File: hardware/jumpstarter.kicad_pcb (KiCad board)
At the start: 4 copper layers, 170 x 170 mm, 148 parts, among them J1 USB_C_Receptacle_PowerOnly_6P, J10 Conn_01x02_Pin, J11 Conn_01x02_Pin, J12 Conn_01x02_Pin, J13 Conn_01x02_Pin, J14 Conn_01x02_Pin, J15 Conn_01x02_Pin, J16 Conn_01x02_Pin, J2 Barrel_Jack_MountingPin, J3 Barrel_Jack_MountingPin, J4 Conn_01x09_Pin, J5 USB_C_Receptacle_PowerOnly_6P, J6 Conn_01x05_Pin, J7 USB3_B, J8 USB3_B_Micro, J9 USB3_A, P1 USB_C_Plug_USB2.0, Q1 FDC6330L, Q2 FDC6330L, Q3 FDC6330L, Q4 FDC6330L, SW1 SW_Push, SW2 SW_Push, SW3 SW_Push, U1 STM32F411CEUx, U2 AP2127N-3.3, U3 AP2127N-3.3, U4 ACS725LLCTR-05AB-T, U6 TMUXHS4212, Y2 25 Mhz Crystal

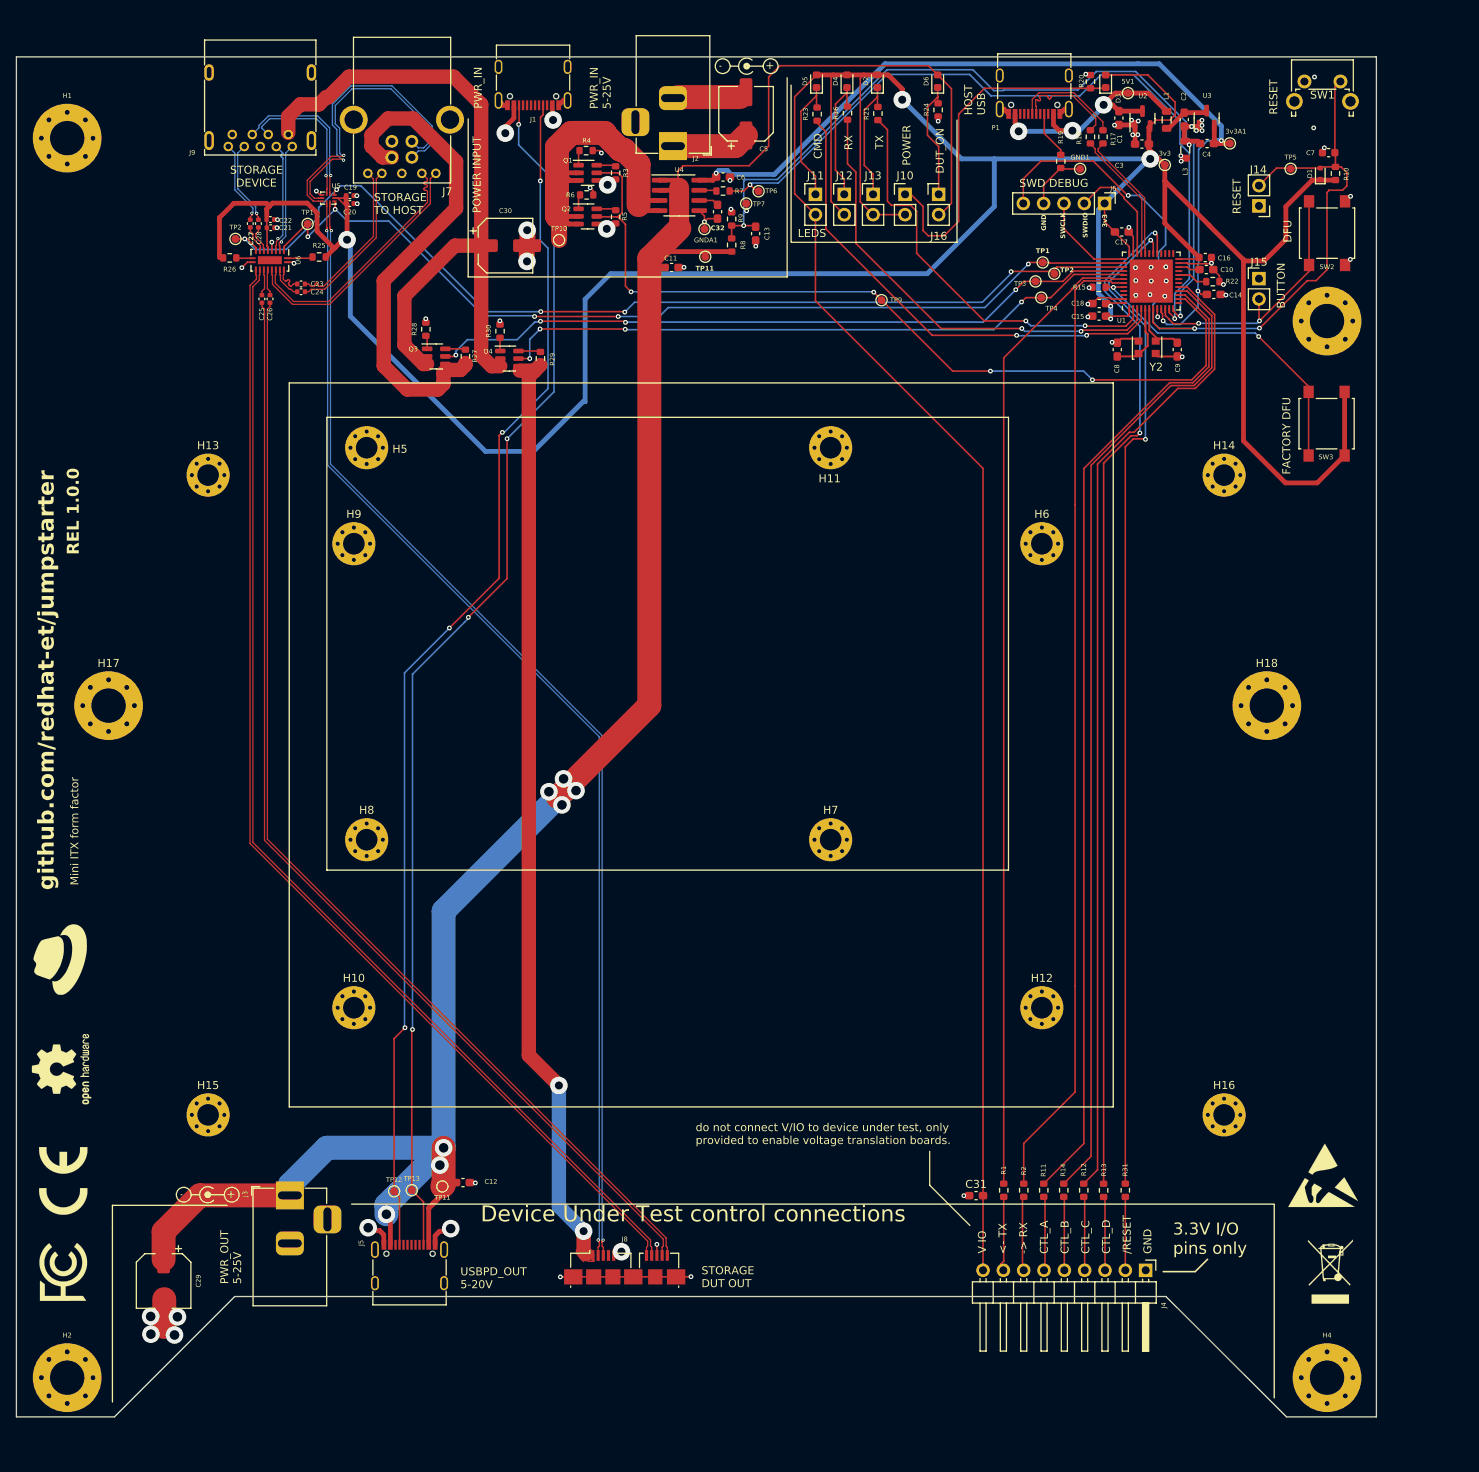
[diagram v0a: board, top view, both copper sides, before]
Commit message: Started routing USB3 diff pairs
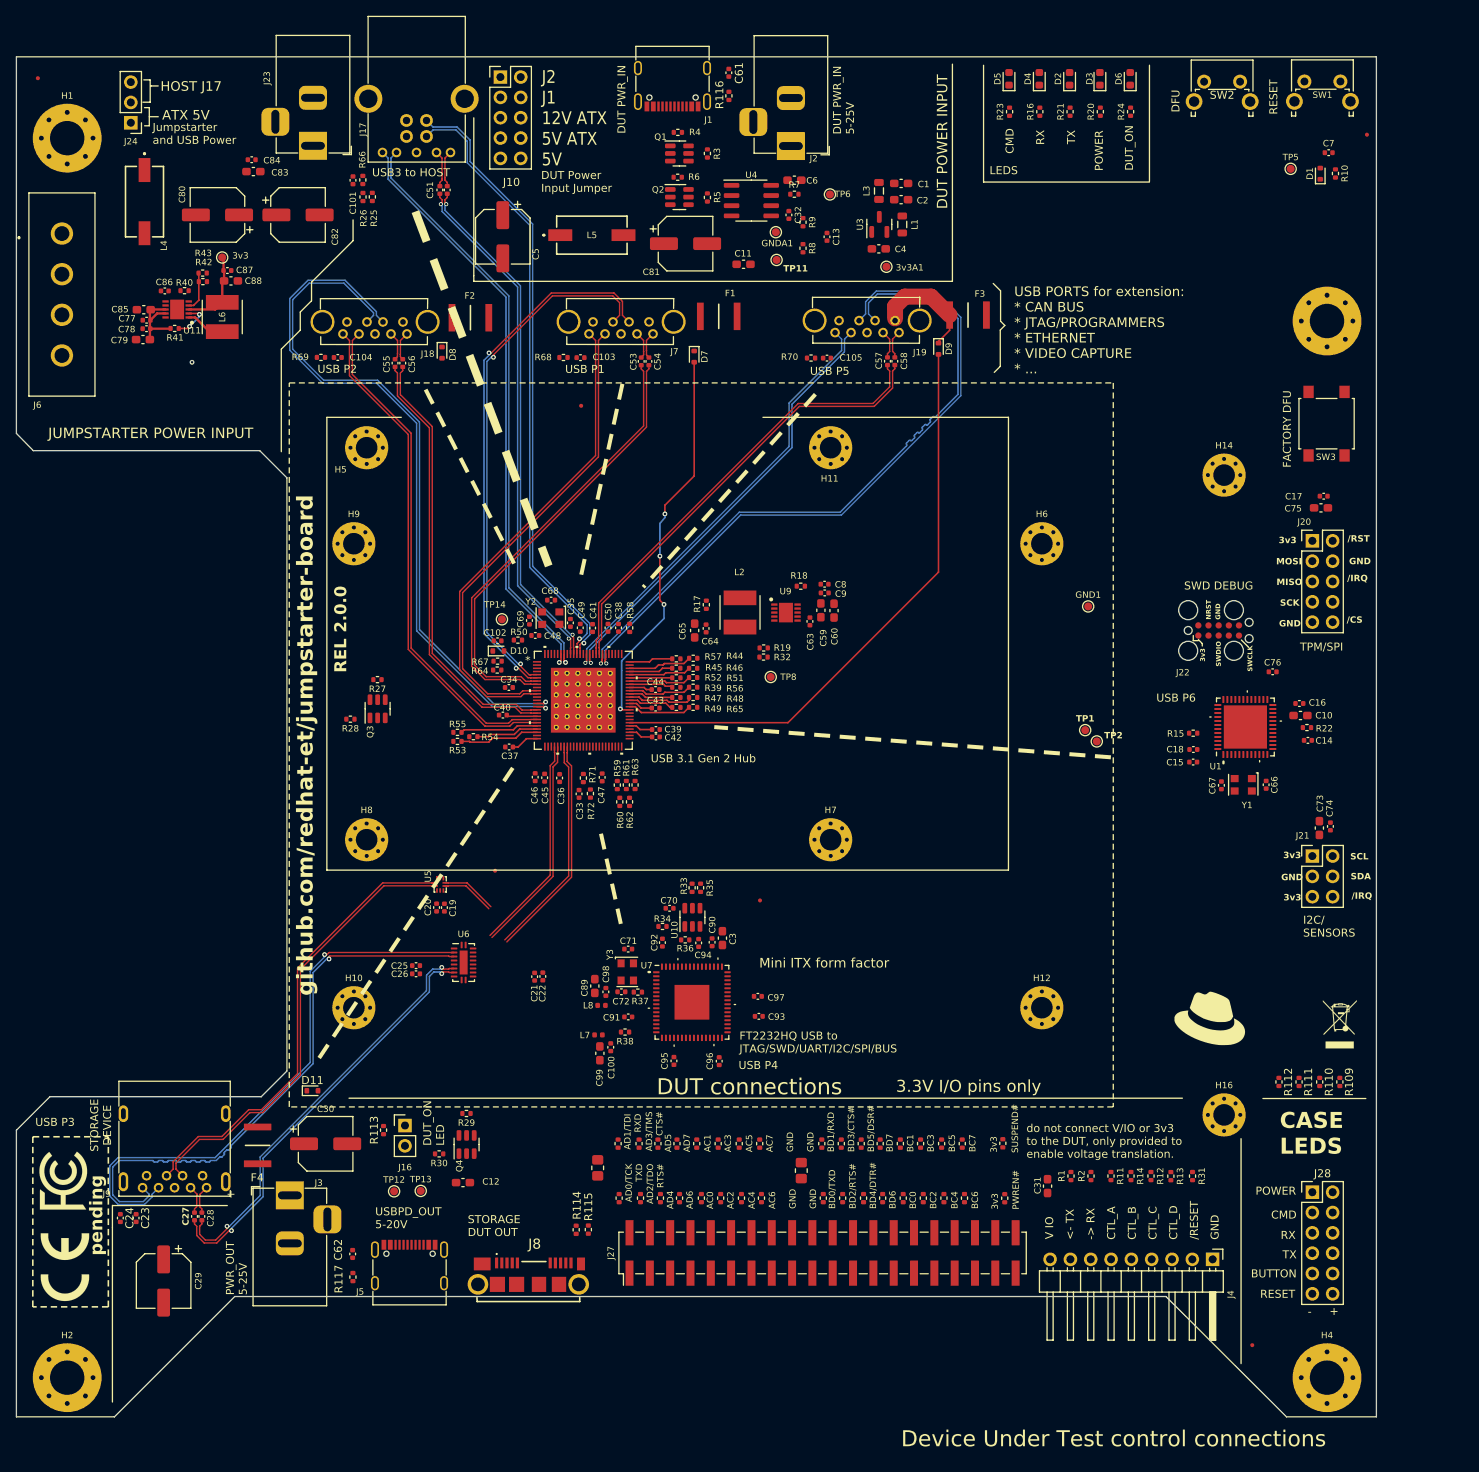
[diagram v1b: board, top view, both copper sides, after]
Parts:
- removed 3v3, 5V1, TP10, TP3, TP4, TP7, TP9: TestPoint, TestPoint:TestPoint_Pad_D1.0mm
- removed H13, H15: Board MountingHole, MountingHole:MountingHole_2.7mm_M2.5_Pad_Via
- removed H17, H18: cable strap hole, MountingHole:MountingHole_4.3mm_M4_Pad_Via
- removed J11, J12, J13, J14, J15: Conn_01x02_Pin, Connector_PinHeader_2.54mm:PinHeader_1x02_P2.54mm_Vertical
- removed P1: USB_C_Plug_USB2.0, Connector_USB:USB_C_Receptacle_G-Switch_GT-USB-7010ASV
- removed the REF** at (81.2, 206.1)
- removed the REF** at (221.6, 215.8)
- removed the REF** at (63.0, 190.5)
- removed the REF** at (220.7, 203.7)
- removed the REF** at (148.6, 65.0)
- removed the TP1 at (93.7, 84.8)
- removed the TP11 at (110.6, 205.1)
- removed the TP2 at (84.7, 86.7)
- removed U2: AP2127N-3.3, Package_TO_SOT_SMD:SOT-23
- added 3v1: TestPoint, TestPoint:TestPoint_Pad_D1.0mm, F.Cu at (83.0, 89.0)
- added C100: 100nF, Capacitor_SMD:C_0402_1005Metric, F.Cu at (131.6, 187.7)
- added C101: 100nF, Capacitor_SMD:C_0402_1005Metric, F.Cu at (99.4, 79.4)
- added C102: 100nF, Capacitor_SMD:C_0402_1005Metric, F.Cu at (117.5, 136.9)
- added C103: 100nF, Capacitor_SMD:C_0402_1005Metric, F.Cu at (127.8, 101.5)
- added C104: 100nF, Capacitor_SMD:C_0402_1005Metric, F.Cu at (97.5, 101.5)
- added C105: 100nF, Capacitor_SMD:C_0402_1005Metric, F.Cu at (158.6, 101.6)
- added C33: 100nF, Capacitor_SMD:C_0402_1005Metric, F.Cu at (127.6, 156.1)
- added C34: 100nF, Capacitor_SMD:C_0402_1005Metric, F.Cu at (118.9, 142.8)
- added C35: 100nF, Capacitor_SMD:C_0402_1005Metric, F.Cu at (126.6, 134.7)
- added C36: 100nF, Capacitor_SMD:C_0402_1005Metric, F.Cu at (125.2, 154.1)
- added C37: 100nF, Capacitor_SMD:C_0402_1005Metric, F.Cu at (118.9, 150.2)
- added C38: 100nF, Capacitor_SMD:C_0402_1005Metric, F.Cu at (132.6, 135.3)
- added C39: 100nF, Capacitor_SMD:C_0402_1005Metric, F.Cu at (137.3, 148.0)
- added C40: 100nF, Capacitor_SMD:C_0402_1005Metric, F.Cu at (118.1, 146.2)
- added C41: 100nF, Capacitor_SMD:C_0402_1005Metric, F.Cu at (129.3, 135.3)
- added C42: 100nF, Capacitor_SMD:C_0402_1005Metric, F.Cu at (137.3, 148.9)
- added C43: 100nF, Capacitor_SMD:C_0402_1005Metric, F.Cu at (137.2, 145.3)
- added C44: 100nF, Capacitor_SMD:C_0402_1005Metric, F.Cu at (137.2, 143.0)
- added C45: 100nF, Capacitor_SMD:C_0402_1005Metric, F.Cu at (123.3, 154.1)
- added C46: 100nF, Capacitor_SMD:C_0402_1005Metric, F.Cu at (122.2, 154.0)
- added C47: 100nF, Capacitor_SMD:C_0402_1005Metric, F.Cu at (130.5, 154.0)
- added C48: 100nF, Capacitor_SMD:C_0402_1005Metric, F.Cu at (122.2, 136.3)
- added C49: 100nF, Capacitor_SMD:C_0402_1005Metric, F.Cu at (127.8, 135.3)
- added C50: 100nF, Capacitor_SMD:C_0402_1005Metric, F.Cu at (131.3, 135.3)
- added C51: 100nF, Capacitor_SMD:C_0402_1005Metric, F.Cu at (110.2, 80.6)
- added C52: 100nF, Capacitor_SMD:C_0402_1005Metric, F.Cu at (111.2, 80.6)
- added C53: 100nF, Capacitor_SMD:C_0402_1005Metric, F.Cu at (135.4, 102.0)
- added C54: 100nF, Capacitor_SMD:C_0402_1005Metric, F.Cu at (136.4, 102.0)
- added C55: 100nF, Capacitor_SMD:C_0402_1005Metric, F.Cu at (104.7, 102.2)
- added C56: 100nF, Capacitor_SMD:C_0402_1005Metric, F.Cu at (105.6, 102.2)
- added C57: 100nF, Capacitor_SMD:C_0402_1005Metric, F.Cu at (166.2, 102.0)
- added C58: 100nF, Capacitor_SMD:C_0402_1005Metric, F.Cu at (167.1, 102.0)
- added C59: 22uF, Capacitor_SMD:C_0603_1608Metric_Pad1.08x0.95mm_HandSolder, F.Cu at (157.9, 133.1)
- added C60: 2.2uF, Capacitor_SMD:C_0603_1608Metric_Pad1.08x0.95mm_HandSolder, F.Cu at (159.5, 133.2)
- added C61: 100nF, Capacitor_SMD:C_0402_1005Metric, F.Cu at (146.4, 65.9)
- added C62: 100nF, Capacitor_SMD:C_0402_1005Metric, F.Cu at (99.3, 213.6)
- added C63: 470pF, Capacitor_SMD:C_0402_1005Metric, F.Cu at (156.5, 134.5)
- added C64: 100nF, Capacitor_SMD:C_0402_1005Metric, F.Cu at (143.5, 135.4)
- added C65: 22uF, Capacitor_SMD:C_0603_1608Metric_Pad1.08x0.95mm_HandSolder, F.Cu at (142.1, 135.7)
- added C66: 12pF, Capacitor_SMD:C_0402_1005Metric, F.Cu at (213.5, 154.9)
- added C67: 12pF, Capacitor_SMD:C_0402_1005Metric, F.Cu at (207.9, 155.0)
- added C68: 12pF, Capacitor_SMD:C_0402_1005Metric, F.Cu at (124.2, 131.9)
- added C69: 12pF, Capacitor_SMD:C_0402_1005Metric, F.Cu at (121.4, 134.4)
- added C70: 100nF, Capacitor_SMD:C_0402_1005Metric, F.Cu at (139.0, 170.4)
- added C71: 27pF, Capacitor_SMD:C_0402_1005Metric, F.Cu at (133.8, 175.5)
- added C72: 27pF, Capacitor_SMD:C_0402_1005Metric, F.Cu at (132.9, 180.8)
- added C73: 1uF, Capacitor_SMD:C_0603_1608Metric_Pad1.08x0.95mm_HandSolder, F.Cu at (220.2, 160.3)
- added C74: 100nF, Capacitor_SMD:C_0402_1005Metric, F.Cu at (221.6, 160.1)
- added C75: 1uF, Capacitor_SMD:C_0603_1608Metric_Pad1.08x0.95mm_HandSolder, F.Cu at (220.4, 120.3)
- added C76: 100nF, Capacitor_SMD:C_0402_1005Metric, F.Cu at (214.3, 140.8)
- added C77: 100nF, Capacitor_SMD:C_0402_1005Metric, F.Cu at (73.6, 96.9)
- added C78: 100nF, Capacitor_SMD:C_0402_1005Metric, F.Cu at (73.6, 97.9)
- added C79: 22uF, Capacitor_SMD:C_0603_1608Metric_Pad1.08x0.95mm_HandSolder, F.Cu at (73.1, 99.3)
- added C80: 47uF 32V, Capacitor_SMD:CP_Elec_6.3x5.4_Nichicon, F.Cu at (82.5, 83.7)
- added C81: 47uF 32V, Capacitor_SMD:CP_Elec_6.3x5.4_Nichicon, F.Cu at (141.0, 87.3)
- added C82: 47uF 32V, Capacitor_SMD:CP_Elec_6.3x5.4_Nichicon, F.Cu at (92.5, 83.7)
- added C83: 1uF, Capacitor_SMD:C_0603_1608Metric_Pad1.08x0.95mm_HandSolder, F.Cu at (86.9, 78.3)
- added C84: 100nF, Capacitor_SMD:C_0402_1005Metric, F.Cu at (86.7, 76.8)
- added C85: 2.2uF, Capacitor_SMD:C_0603_1608Metric_Pad1.08x0.95mm_HandSolder, F.Cu at (73.2, 95.5)
- added C86: 470pF, Capacitor_SMD:C_0402_1005Metric, F.Cu at (75.9, 93.2)
- added C87: 100nF, Capacitor_SMD:C_0402_1005Metric, F.Cu at (83.7, 90.7)
- added C88: 22uF, Capacitor_SMD:C_0603_1608Metric_Pad1.08x0.95mm_HandSolder, F.Cu at (84.1, 92.0)
- added C89: 4.7uF, Capacitor_SMD:C_0603_1608Metric_Pad1.08x0.95mm_HandSolder, F.Cu at (129.6, 180.1)
- added C90: 100nF, Capacitor_SMD:C_0402_1005Metric, F.Cu at (144.3, 174.6)
- added C91: 100nF, Capacitor_SMD:C_0402_1005Metric, F.Cu at (133.8, 183.9)
- added C92: 100nF, Capacitor_SMD:C_0402_1005Metric, F.Cu at (138.1, 174.7)
- added C93: 100nF, Capacitor_SMD:C_0402_1005Metric, F.Cu at (150.1, 183.9)
- added C94: 100nF, Capacitor_SMD:C_0402_1005Metric, F.Cu at (142.6, 174.7)
- added C95: 100nF, Capacitor_SMD:C_0402_1005Metric, F.Cu at (139.5, 189.4)
- added C96: 100nF, Capacitor_SMD:C_0402_1005Metric, F.Cu at (145.2, 189.5)
- added C97: 100nF, Capacitor_SMD:C_0402_1005Metric, F.Cu at (150.0, 181.4)
- added C98: 100nF, Capacitor_SMD:C_0402_1005Metric, F.Cu at (131.0, 180.8)
- added C99: 4.7uF, Capacitor_SMD:C_0603_1608Metric_Pad1.08x0.95mm_HandSolder, F.Cu at (130.2, 188.5)
- added D10: 1N4148WT, Diode_SMD:D_SOD-523, F.Cu at (117.6, 138.2)
- added D11: 1N4448WT, Diode_SMD:D_SOD-523, F.Cu at (94.3, 193.2)
- added D7: 1N4448WT, Diode_SMD:D_SOD-523, F.Cu at (142.0, 101.4)
- added D8: 1N4448WT, Diode_SMD:D_SOD-523, F.Cu at (110.5, 100.9)
- added D9: 1N4448WT, Diode_SMD:D_SOD-523, F.Cu at (172.6, 100.4)
- added F1: MF-MSMF125-2, FOOTPRINTS:MF-MSMF125-2, F.Cu at (145.1, 96.4)
- added F2: MF-MSMF125-2, FOOTPRINTS:MF-MSMF125-2, F.Cu at (114.1, 96.5)
- added F3: MF-MSMF125-2, FOOTPRINTS:MF-MSMF125-2, F.Cu at (176.3, 96.2)
- added F4: MF-MSMF125-2, FOOTPRINTS:MF-MSMF125-2, F.Cu at (87.5, 200.0)
- added FID1: Fiducial, Fiducial:Fiducial_0.5mm_Mask1mm, F.Cu at (60.0, 66.6)
- added FID2: Fiducial, Fiducial:Fiducial_0.5mm_Mask1mm, F.Cu at (127.9, 107.6)
- added FID3: Fiducial, Fiducial:Fiducial_0.5mm_Mask1mm, F.Cu at (211.8, 225.0)
- added FID4: Fiducial, Fiducial:Fiducial_0.5mm_Mask1mm, F.Cu at (150.3, 169.4)
- added FID5: Fiducial, Fiducial:Fiducial_0.5mm_Mask1mm, F.Cu at (226.1, 73.7)
- added FID6: Fiducial, Fiducial:Fiducial_0.5mm_Mask1mm, F.Cu at (117.1, 165.7)
- added J17: USB3_B, USB3Wurth:Wurth WR-COM USB 3.0 692221030100, F.Cu at (107.3, 71.9)
- added J18: USB3_A, Connector_USB:SS-52000-004, F.Cu at (108.7, 97.1)
- added J19: USB3_A, Connector_USB:SS-52000-004, F.Cu at (170.2, 96.9)
- added J20: SPI/TPM connector, Connector_PinHeader_2.54mm:PinHeader_2x05_P2.54mm_Vertical, F.Cu at (219.3, 124.4)
- added J21: I2C connector, Connector_PinHeader_2.54mm:PinHeader_2x03_P2.54mm_Vertical, F.Cu at (219.3, 163.8)
- added J22: NC, Connector:Tag-Connect_TC2050-IDC-FP_2x05_P1.27mm_Vertical, F.Cu at (207.6, 135.6)
- added J23: DNM, Connector_BarrelJack:BarrelJack_Horizontal, F.Cu at (94.4, 75.1)
- added J24: Conn_01x03_Pin, Connector_PinHeader_2.54mm:PinHeader_1x03_P2.54mm_Vertical, F.Cu at (71.6, 72.2)
- added J27: Conn_02x20_Odd_Even, Connector_PinHeader_2.54mm:PinHeader_2x20_P2.54mm_Vertical_SMD, F.Cu at (158.1, 213.5)
- added J28: CASE CONNECTORS, Connector_PinHeader_2.54mm:PinHeader_2x06_P2.54mm_Vertical, F.Cu at (219.3, 205.9)
- added L2: 1.5uH, FOOTPRINTS:LQH5BPB100MT0L, F.Cu at (147.8, 133.4)
- added L4: 7427932, FOOTPRINTS:7427932, F.Cu at (73.3, 82.0)
- added L5: 7427932, FOOTPRINTS:7427932, F.Cu at (129.2, 86.2)
- added L6: 1.5uH, FOOTPRINTS:LQH5BPB100MT0L, F.Cu at (83.0, 96.5)
- added L7: 120Ω@100MH, Inductor_SMD:L_0402_1005Metric, F.Cu at (130.1, 186.2)
- added L8: 120Ω@100MH, Inductor_SMD:L_0402_1005Metric, F.Cu at (130.5, 182.5)
- added R100: 100, Resistor_SMD:R_0402_1005Metric, F.Cu at (170.3, 199.8)
- added R101: 100, Resistor_SMD:R_0402_1005Metric, F.Cu at (173.3, 206.6)
- added R102: 100, Resistor_SMD:R_0402_1005Metric, F.Cu at (173.0, 199.8)
- added R103: 100, Resistor_SMD:R_0402_1005Metric, F.Cu at (175.8, 206.6)
- added R104: 100, Resistor_SMD:R_0402_1005Metric, F.Cu at (175.6, 199.8)
- added R105: 100, Resistor_SMD:R_0402_1005Metric, F.Cu at (180.9, 206.6)
- added R106: 100, Resistor_SMD:R_0402_1005Metric, F.Cu at (180.6, 199.8)
- added R107: NC, Resistor_SMD:R_0805_2012Metric_Pad1.20x1.40mm_HandSolder, F.Cu at (130.0, 202.8)
- added R108: NC, Resistor_SMD:R_0805_2012Metric_Pad1.20x1.40mm_HandSolder, F.Cu at (155.4, 203.2)
- added R109: 470, Resistor_SMD:R_0402_1005Metric, F.Cu at (222.8, 192.1)
- added R110: 470, Resistor_SMD:R_0402_1005Metric, F.Cu at (220.2, 192.1)
- added R111: 470, Resistor_SMD:R_0402_1005Metric, F.Cu at (217.7, 192.1)
- added R112: 470, Resistor_SMD:R_0402_1005Metric, F.Cu at (215.1, 192.1)
- added R113: 2k, Resistor_SMD:R_0402_1005Metric, F.Cu at (103.2, 198.1)
- added R114: 330, Resistor_SMD:R_0402_1005Metric, F.Cu at (127.3, 210.6)
- added R115: 330, Resistor_SMD:R_0402_1005Metric, F.Cu at (128.8, 210.5)
- added R116: 330, Resistor_SMD:R_0402_1005Metric, F.Cu at (146.4, 68.8)
- added R117: 330, Resistor_SMD:R_0402_1005Metric, F.Cu at (99.4, 216.5)
- added R32: 12k, Resistor_SMD:R_0402_1005Metric, F.Cu at (150.7, 139.0)
- added R33: 10k, Resistor_SMD:R_0402_1005Metric, F.Cu at (141.8, 167.8)
- added R34: 10k, Resistor_SMD:R_0402_1005Metric, F.Cu at (138.1, 172.6)
- added R35: 10k, Resistor_SMD:R_0402_1005Metric, F.Cu at (142.8, 167.8)
- added R36: 2k, Resistor_SMD:R_0402_1005Metric, F.Cu at (140.9, 174.3)
- added R37: 12k, Resistor_SMD:R_0402_1005Metric, F.Cu at (135.0, 180.8)
- added R38: 2k, Resistor_SMD:R_0402_1005Metric, F.Cu at (133.4, 185.8)
- added R39: 10k, Resistor_SMD:R_0402_1005Metric, F.Cu at (139.8, 142.8)
- added R40: 10k, Resistor_SMD:R_0402_1005Metric, F.Cu at (78.3, 93.2)
- added R41: 10k, Resistor_SMD:R_0402_1005Metric, F.Cu at (77.1, 97.9)
- added R42: 22k, Resistor_SMD:R_0402_1005Metric, F.Cu at (80.6, 92.0)
- added R43: 5k1, Resistor_SMD:R_0402_1005Metric, F.Cu at (80.6, 91.0)
- added R44: 10k, Resistor_SMD:R_0402_1005Metric, F.Cu at (141.9, 139.1)
- added R45: 10k, Resistor_SMD:R_0402_1005Metric, F.Cu at (139.8, 140.4)
- added R46: 10k, Resistor_SMD:R_0402_1005Metric, F.Cu at (141.9, 140.4)
- added R47: 10k, Resistor_SMD:R_0402_1005Metric, F.Cu at (139.8, 144.0)
- added R48: 10k, Resistor_SMD:R_0402_1005Metric, F.Cu at (141.9, 144.0)
- added R49: 10k, Resistor_SMD:R_0402_1005Metric, F.Cu at (139.8, 145.3)
- added R50: 12k 1%, Resistor_SMD:R_0402_1005Metric, F.Cu at (120.0, 136.9)
- added R51: 200K, Resistor_SMD:R_0402_1005Metric, F.Cu at (141.9, 141.5)
- added R52: 200K, Resistor_SMD:R_0402_1005Metric, F.Cu at (139.8, 141.6)
- added R53: 200K, Resistor_SMD:R_0402_1005Metric, F.Cu at (112.5, 149.5)
- added R54: 200K, Resistor_SMD:R_0402_1005Metric, F.Cu at (114.4, 148.9)
- added R55: 10K, Resistor_SMD:R_0402_1005Metric, F.Cu at (112.5, 148.4)
- added R56: 10k, Resistor_SMD:R_0402_1005Metric, F.Cu at (141.9, 142.7)
- added R57: NC 10k, Resistor_SMD:R_0402_1005Metric, F.Cu at (139.8, 139.2)
- added R58: NC 10k, Resistor_SMD:R_0402_1005Metric, F.Cu at (134.0, 135.3)
- added R59: 200K, Resistor_SMD:R_0402_1005Metric, F.Cu at (132.4, 155.0)
- added R60: 200K, Resistor_SMD:R_0402_1005Metric, F.Cu at (132.7, 157.1)
- added R61: 200K, Resistor_SMD:R_0402_1005Metric, F.Cu at (133.6, 155.0)
- added R62: 200K, Resistor_SMD:R_0402_1005Metric, F.Cu at (134.0, 157.1)
- added R63: 200K, Resistor_SMD:R_0402_1005Metric, F.Cu at (134.6, 155.0)
- added R64: NC 10k, Resistor_SMD:R_0402_1005Metric, F.Cu at (117.4, 140.6)
- added R65: NC 10k, Resistor_SMD:R_0402_1005Metric, F.Cu at (141.9, 145.3)
- added R66: 330, Resistor_SMD:R_0402_1005Metric, F.Cu at (100.6, 79.3)
- added R67: 10k, Resistor_SMD:R_0402_1005Metric, F.Cu at (117.5, 139.5)
- added R68: 330, Resistor_SMD:R_0402_1005Metric, F.Cu at (125.7, 101.5)
- added R69: 330, Resistor_SMD:R_0402_1005Metric, F.Cu at (95.4, 101.5)
- added R70: 330, Resistor_SMD:R_0402_1005Metric, F.Cu at (156.7, 101.6)
- added R71: 200K, Resistor_SMD:R_0402_1005Metric, F.Cu at (128.2, 154.1)
- added R72: 200K, Resistor_SMD:R_0402_1005Metric, F.Cu at (129.1, 156.0)
- added R73: 100, Resistor_SMD:R_0402_1005Metric, F.Cu at (132.7, 206.6)
- added R74: 100, Resistor_SMD:R_0402_1005Metric, F.Cu at (132.5, 199.8)
- added R75: 100, Resistor_SMD:R_0402_1005Metric, F.Cu at (135.3, 206.6)
- added R76: 100, Resistor_SMD:R_0402_1005Metric, F.Cu at (135.2, 199.8)
- added R77: 100, Resistor_SMD:R_0402_1005Metric, F.Cu at (137.8, 206.6)
- added R78: 100, Resistor_SMD:R_0402_1005Metric, F.Cu at (137.5, 199.8)
- added R79: 100, Resistor_SMD:R_0402_1005Metric, F.Cu at (140.2, 206.6)
- added R80: 100, Resistor_SMD:R_0402_1005Metric, F.Cu at (139.9, 199.8)
- added R81: 100, Resistor_SMD:R_0402_1005Metric, F.Cu at (142.9, 206.6)
- added R82: 100, Resistor_SMD:R_0402_1005Metric, F.Cu at (142.4, 199.8)
- added R83: 100, Resistor_SMD:R_0402_1005Metric, F.Cu at (145.3, 206.6)
- added R84: 100, Resistor_SMD:R_0402_1005Metric, F.Cu at (145.0, 199.8)
- added R85: 100, Resistor_SMD:R_0402_1005Metric, F.Cu at (147.9, 206.6)
- added R86: 100, Resistor_SMD:R_0402_1005Metric, F.Cu at (147.7, 199.8)
- added R87: 100, Resistor_SMD:R_0402_1005Metric, F.Cu at (150.4, 206.6)
- added R88: 100, Resistor_SMD:R_0402_1005Metric, F.Cu at (150.2, 199.8)
- added R89: 100, Resistor_SMD:R_0402_1005Metric, F.Cu at (158.2, 206.6)
- added R90: 100, Resistor_SMD:R_0402_1005Metric, F.Cu at (158.0, 199.8)
- added R91: 100, Resistor_SMD:R_0402_1005Metric, F.Cu at (160.6, 206.6)
- added R92: 100, Resistor_SMD:R_0402_1005Metric, F.Cu at (160.4, 199.8)
- added R93: 100, Resistor_SMD:R_0402_1005Metric, F.Cu at (163.2, 206.6)
- added R94: 100, Resistor_SMD:R_0402_1005Metric, F.Cu at (162.9, 199.8)
- added R95: 100, Resistor_SMD:R_0402_1005Metric, F.Cu at (165.6, 206.6)
- added R96: 100, Resistor_SMD:R_0402_1005Metric, F.Cu at (165.3, 199.8)
- added R97: 100, Resistor_SMD:R_0402_1005Metric, F.Cu at (168.2, 206.6)
- added R98: 100, Resistor_SMD:R_0402_1005Metric, F.Cu at (167.8, 199.8)
- added R99: 100, Resistor_SMD:R_0402_1005Metric, F.Cu at (170.7, 206.6)
- added REF**: WEEE-Logo_4.2x6mm_SilkScreen, Symbol:WEEE-Logo_4.2x6mm_SilkScreen, F.Cu at (222.7, 184.9)
- added TP14: TestPoint, TestPoint:TestPoint_Pad_D1.0mm, F.Cu at (118.0, 134.3)
- added TP8: TestPoint, TestPoint:TestPoint_Pad_D1.0mm, F.Cu at (151.6, 141.5)
- added U10: 93LC56BT-E/OT, Package_TO_SOT_SMD:SOT-23-6, F.Cu at (141.8, 171.5)
- added U11: MIC23201YML, FOOTPRINTS:SON50P300X300X100-11N-D, F.Cu at (77.4, 95.5)
- added U7: FT2232HQ, Package_DFN_QFN:QFN-64-1EP_9x9mm_P0.5mm_EP4.35x4.35mm, F.Cu at (141.8, 182.1)
- added U8: USB7206CT/KDX, VQFN100:VQFN100_KDX_MCH, F.Cu at (128.2, 144.4)
- added U9: MIC23201YML, FOOTPRINTS:SON50P300X300X100-11N-D, F.Cu at (153.5, 133.4)
- added Y1: 25 Mhz Crystal +/- 10ppm, Oscillator:Oscillator_SMD_EuroQuartz_XO32-4Pin_3.2x2.5mm, F.Cu at (210.7, 154.9)
- added Y3: 12MHz crystal +/- 30ppm max 12pf, Oscillator:Oscillator_SMD_EuroQuartz_XO32-4Pin_3.2x2.5mm, F.Cu at (133.7, 178.3)
- C13, C14, C15, C17, C18, C32: footprint Capacitor_SMD:C_0603_1608Metric_Pad1.08x0.95mm_HandSolder -> Capacitor_SMD:C_0402_1005Metric
- C16, C7: footprint Capacitor_SMD:C_0603_1608Metric -> Capacitor_SMD:C_0402_1005Metric
- C3: value 1uF -> 3.3uF
- C8, C9: value 12pF -> 100nF; footprint Capacitor_SMD:C_0603_1608Metric_Pad1.08x0.95mm_HandSolder -> Capacitor_SMD:C_0402_1005Metric
- J10: value Conn_01x02_Pin -> SPI/TPM connector; footprint Connector_PinHeader_2.54mm:PinHeader_1x02_P2.54mm_Vertical -> Connector_PinHeader_2.54mm:PinHeader_2x05_P2.54mm_Vertical
- J6: value Conn_01x05_Pin -> Molex 4 Pin Peripheral Power Connector; footprint Connector_PinHeader_2.54mm:PinHeader_1x05_P2.54mm_Vertical -> FOOTPRINTS:3502111
- J7: value USB3_B -> USB3_A; footprint USB3Wurth:Wurth WR-COM USB 3.0 692221030100 -> Connector_USB:SS-52000-004
- J8: value USB3_B_Micro -> Hirose USB3_B_Micro; footprint Connector_USB:USB3_Micro-B_Connfly_DS1104-01 -> FOOTPRINTS:ZX360DB10P30
- R1, R10, R11, R12, R13, R14, R15, R2, R22, R24, R27, R28, R29, R3, R30, R31, R4, R5, R6, R7, R8, R9: footprint Resistor_SMD:R_0603_1608Metric -> Resistor_SMD:R_0402_1005Metric
- R16, R20, R21, R23: value 1k -> 470; footprint Resistor_SMD:R_0603_1608Metric -> Resistor_SMD:R_0402_1005Metric
- R17, R18: value 10 -> 10k; footprint Resistor_SMD:R_0603_1608Metric -> Resistor_SMD:R_0402_1005Metric
- R19: value 5k1 -> 10k; footprint Resistor_SMD:R_0603_1608Metric -> Resistor_SMD:R_0402_1005Metric
- R25: value 0 -> 43K; footprint Resistor_SMD:R_0603_1608Metric -> Resistor_SMD:R_0402_1005Metric
- R26: value 0 -> 49K9; footprint Resistor_SMD:R_0603_1608Metric -> Resistor_SMD:R_0402_1005Metric
- SW2: footprint Button_Switch_SMD:SW_SPST_B3S-1000 -> Button_Switch_THT:SW_Tactile_SPST_Angled_PTS645Vx58-2LFS
- Y2: value 25 Mhz Crystal -> 25 Mhz Crystal +/- 10ppm
- moved G*** 144.4 mm to (207.0, 184.1), turned to 0 degrees
- moved J16 134.2 mm to (105.9, 197.5)
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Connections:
- net /USB_STORAGE_MUX/_STORAGE_SSRXN renamed /USB_STORAGE_MUX/_STORAGE_SSTXN
- net /USB_STORAGE_MUX/_STORAGE_SSRXP renamed /USB_STORAGE_MUX/_STORAGE_SSTXP
- C23 pad 1: /USB_STORAGE_MUX/HOST_SSRXP -> Net-(J9-SHIELD)
- C23 pad 2: /USB_STORAGE_MUX/_HOST_SSRXP -> GND
- C24 pad 1: /USB_STORAGE_MUX/HOST_SSRXN -> Net-(J8-SHIELD)
- C24 pad 2: /USB_STORAGE_MUX/_HOST_SSRXN -> GND
- C27 pad 2: /USB_STORAGE_MUX/STORAGE_SSRXN -> /USB_STORAGE_MUX/STORAGE_SSTXN
- C28 pad 2: /USB_STORAGE_MUX/STORAGE_SSRXP -> /USB_STORAGE_MUX/STORAGE_SSTXP
- C3 pad 1: +3.3V -> +1V8
- C5 pad 1: VCC -> /board_control/_VCC
- C8 pad 1: GND -> +5V
- C8 pad 2: /XTALO -> GND
- C9 pad 1: GND -> +5V
- C9 pad 2: /XTALI -> GND
- J1 pad A9: VCC -> /board_control/J1_VCC
- J1 pad B9: VCC -> /board_control/J1_VCC
- J1 pad S1: GND -> Net-(J1-SHIELD)
- J10 pad 1: Net-(D3-K) -> /board_control/J2_VCC
- J10 pad 2: +3.3V -> /board_control/_VCC
- J16 pad 1: Net-(D6-K) -> Net-(J16-Pin_1)
- J2 pad 1: VCC -> /board_control/J2_VCC
- J5 pad S1: GND -> Net-(J5-SHIELD)
- J6 pad 1: +3.3V -> /Power/12V_IN
- J6 pad 2: /SWDIO -> GND
- J6 pad 3: /SWCLK -> GND
- J6 pad 4: GND -> /Power/5V_IN
- J7 pad 1: /USB_STORAGE_MUX/VBUS_HOST -> Net-(D7-K)
- J7 pad 10: GND -> Net-(J7-SHIELD)
- J7 pad 2: /USB_STORAGE_MUX/HOST_DN -> /USB 3.2 Gen2 front-hub/P1_DN
- J7 pad 3: /USB_STORAGE_MUX/HOST_DP -> /USB 3.2 Gen2 front-hub/P1_DP
- J7 pad 5: /USB_STORAGE_MUX/HOST_SSTXN -> /USB 3.2 Gen2 front-hub/P1_SSRXN
- J7 pad 6: /USB_STORAGE_MUX/HOST_SSTXP -> /USB 3.2 Gen2 front-hub/P1_SSRXP
- J7 pad 8: /USB_STORAGE_MUX/HOST_SSRXN -> /USB 3.2 Gen2 front-hub/P1_SSTXN
- J7 pad 9: /USB_STORAGE_MUX/HOST_SSRXP -> /USB 3.2 Gen2 front-hub/P1_SSTXP
- J8 pad 11: GND -> Net-(J8-SHIELD)
- J9 pad 1: /USB_STORAGE_MUX/VBUS_STORAGE -> /USB_STORAGE_MUX/VBUS_STORAGE_
- J9 pad 10: GND -> Net-(J9-SHIELD)
- L1 pad 1: +5VA -> GNDA
- L1 pad 2: +5V -> GND
- L3 pad 1: GNDA -> +5VA
- L3 pad 2: GND -> +5V
- Q3 pad 4: /USB_STORAGE_MUX/VBUS_HOST -> +5V
- R17 pad 1: /DN -> VCORE
- R17 pad 2: /_DN -> Net-(U9-PG)
- R18 pad 1: /DP -> +5V
- R18 pad 2: /_DP -> Net-(U9-EN)
- R19 pad 1: Net-(P1-CC) -> VCORE
- R19 pad 2: GND -> /Power/FBVCORE
- R25 pad 1: Net-(U6-RSVD1) -> /USB 3.2 Gen2 front-hub/VBUS_MON_UP
- R25 pad 2: +3.3V -> /Power/VBUS_UPSTREAM
- R26 pad 1: Net-(U6-RSVD2) -> GND
- R26 pad 2: +3.3V -> /USB 3.2 Gen2 front-hub/VBUS_MON_UP
- R27 pad 1: /USB_STORAGE_MUX/VBUS_HOST -> +5V
- U1 pad 13: unconnected-(U1-PA3-Pad13) -> /FT2232_EECLK
- U1 pad 18: unconnected-(U1-PB0-Pad18) -> /nRESET_OUT
- U1 pad 19: unconnected-(U1-PB1-Pad19) -> /FT2232_EECS
- U1 pad 21: unconnected-(U1-PB10-Pad21) -> /IRQ_IN
- U1 pad 25: unconnected-(U1-PB12-Pad25) -> /SPI2_NSS
- U1 pad 26: unconnected-(U1-PB13-Pad26) -> /SPI2_SCK
- U1 pad 27: unconnected-(U1-PB14-Pad27) -> /SPI2_MISO
- U1 pad 28: unconnected-(U1-PB15-Pad28) -> /SPI2_MOSI
- U1 pad 31: unconnected-(U1-PA10-Pad31) -> /FT2232_EEDATA
- U1 pad 45: unconnected-(U1-PB8-Pad45) -> /I2C1_SCL
- U1 pad 46: unconnected-(U1-PB9-Pad46) -> /I2C1_SDA
- U1 pad 5: /XTALO -> /XTALI
- U1 pad 6: /XTALI -> /XTALO
- U5 pad 4: /USB_STORAGE_MUX/HOST_DN -> /SHOST_DN
- U5 pad 5: /USB_STORAGE_MUX/HOST_DP -> /SHOST_DP
- U6 pad 1: Net-(U6-RSVD1) -> +3.3V
- U6 pad 10: Net-(U6-RSVD2) -> +3.3V
- U6 pad 16: /USB_STORAGE_MUX/HOST_SSTXN -> /SHOST_SSTXN
- U6 pad 17: /USB_STORAGE_MUX/HOST_SSTXP -> /SHOST_SSTXP
- U6 pad 18: /USB_STORAGE_MUX/_HOST_SSRXN -> /SHOST_SSRXP
- U6 pad 19: /USB_STORAGE_MUX/_HOST_SSRXP -> /SHOST_SSRXN
- U6 pad 3: /USB_STORAGE_MUX/STORAGE_SSTXP -> /USB_STORAGE_MUX/STORAGE_SSRXP
- U6 pad 4: /USB_STORAGE_MUX/STORAGE_SSTXN -> /USB_STORAGE_MUX/STORAGE_SSRXN
- Y2 pad 1: /XTALO -> /USB 3.2 Gen2 front-hub/XTALO
- Y2 pad 3: /XTALI -> /USB 3.2 Gen2 front-hub/XTALI
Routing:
- net +3.3V: track 567.5 -> 19.3 mm, vias 5 -> 0
- net /board_control/VCCOUT: track 284.2 -> 0.00 mm, vias 7 -> 0
- net /board_control/CC2: track 152.3 -> 0.00 mm, vias 4 -> 0
- net /board_control/CC1: track 151.4 -> 0.00 mm, vias 4 -> 0
- net /USB_STORAGE_MUX/DUT_SSTXP: track 144.2 -> 0.00 mm
- net /USB_STORAGE_MUX/DUT_SSTXN: track 144.2 -> 0.00 mm
- net /USB_STORAGE_MUX/DUT_SSRXP: track 139.9 -> 0.00 mm
- net /USB_STORAGE_MUX/DUT_SSRXN: track 139.9 -> 0.00 mm
- net /USB_STORAGE_MUX/DUT_DN: track 146.3 -> 6.71 mm, vias 2 -> 0
- net /USB_STORAGE_MUX/DUT_DP: track 146.2 -> 7.01 mm, vias 2 -> 0
- net GNDA: track 136.4 -> 0.00 mm, vias 10 -> 0
- net /CTL_D: track 128.5 -> 0.00 mm, vias 2 -> 0
- net /USB_SEL: track 127.6 -> 0.00 mm, vias 5 -> 0
- net /RESET: track 125.8 -> 0.00 mm, vias 2 -> 0
- net /CTL_A: track 123.4 -> 0.00 mm
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- removed copper zone on F.Cu, net /USB_STORAGE_MUX/VBUS_DUT
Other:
- outline, holes or cut-outs redrawn
- board text added: "/CS"
- board text added: "/IRQ"
- board text added: "/RST"
- board text added: "AC0"
- board text added: "AC1"
- board text added: "AC2"
- board text added: "AC3"
- board text added: "AC4"
- board text added: "AC5"
- board text added: "AC6"
- board text added: "AC7"
- board text added: "AD0/TCK TXD"
- board text added: "AD1/TDI RXD"
- board text added: "AD2/TDO RTS#"
- board text added: "AD3/TMS CTS#"
- board text added: "AD4"
- board text added: "AD5"
- board text added: "AD6"
- board text added: "AD7"
- board text added: "ATX 5V"
- board text added: "BC0"
- board text added: "BC1"
- board text added: "BC2"
- board text added: "BC3"
- board text added: "BC4"
- board text added: "BC5"
- board text added: "BC6"
- board text added: "BC7"
- board text added: "BD0/TXD"
- board text added: "BD1/RXD"
- board text added: "BD2/RTS#"
- board text added: "BD3/CTS#"
- board text added: "BD4/DTR#"
- board text added: "BD5/DSR#"
- board text added: "BD6"
- board text added: "BD7"
- board text added: "CASE LEDS"
- board text added: "DUT POWER INPUT"
- board text added: "DUT PWR_IN"
- board text added: "DUT PWR_IN 5-25V"
- board text added: "DUT Power Input Jumper"
- board text added: "DUT connections"
- board text added: "DUT_ON LED"
- board text added: "FT2232HQ USB to JTAG/SWD/UART/I2C/SPI/BUS"
- board text added: "HOST J17"
- board text added: "I2C/ SENSORS"
- board text added: "J2 J1 12V ATX 5V ATX 5V"
- board text added: "JUMPSTARTER POWER INPUT"
- board text added: "Jumpstarter and USB Power"
- board text added: "MISO"
- board text added: "MOSI"
- board text added: "NRST"
- board text added: "PWREN#"
- board text added: "REL 2.0.0"
- board text added: "SCK"
- board text added: "SCL"
- board text added: "SDA"
- board text added: "SUSPEND#"
- board text added: "TPM/SPI"
- board text added: "USB 3.1 Gen 2 Hub"
- board text added: "USB P1"
- board text added: "USB P2"
- board text added: "USB P3"
- board text added: "USB P4"
- board text added: "USB P5"
- board text added: "USB P6"
- board text added: "USB PORTS for extension: * CAN BUS * JTAG/PROGRAMMERS * ETHERNET * VIDEO CAPTURE * ..."
- board text added: "USB3 to HOST"
- board text added: "do not connect V/IO or 3v3 to the DUT, only provided to enable voltage translation."
- board text added: "github.com/redhat-et/jumpstarter-board"
- board text added: "pending"
- board text removed: "HOST USB"
- board text removed: "POWER INPUT"
- board text removed: "PWR_IN"
- board text removed: "PWR_IN 5-25V"
- board text removed: "REL 1.0.0"
- board text removed: "STORAGE TO HOST"
- board text removed: "do not connect V/IO to device under test, only provided to enable voltage translation boards."
- board text removed: "github.com/redhat-et/jumpstarter"

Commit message: Routing and several design fixes
Signed-off-by: Miguel Angel Ajo Pelayo <majopela@redhat.com>
Signed-off-by: Ricardo Noriega <rnoriega@redhat.com>
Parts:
- added R118: NC 10k, Resistor_SMD:R_0402_1005Metric, F.Cu at (178.1, 197.6)
- R37: value 12k -> 12k 1%
- R57, R58, R65: value NC 10k -> 10k
- moved C24 61.0 mm to (131.3, 210.7), turned to 90 degrees
- moved R114 56.0 mm to (71.4, 208.8), turned to 90 degrees
- moved C25 39.1 mm to (125.8, 211.9), turned to 90 degrees
- moved C26 38.6 mm to (126.7, 211.9), turned to 90 degrees
- moved C17 29.7 mm to (204.7, 143.8), turned to 0 degrees
- moved C29 28.9 mm to (98.6, 199.4), turned to 90 degrees
- moved F4 24.0 mm to (70.8, 217.3)
- moved C30 23.6 mm to (78.9, 216.1)
- moved C76 20.2 mm to (220.5, 121.6)
- moved J10 14.7 mm to (129.5, 75.3), turned to -90 degrees
- moved C84 14.2 mm to (88.8, 90.8)
- moved C83 14.2 mm to (89.0, 92.3)
- moved C22 11.3 mm to (113.2, 173.5), turned to 0 degrees
- moved C21 9.12 mm to (113.2, 180.8), turned to 0 degrees
- moved D11 8.91 mm to (86.9, 198.1), turned to 90 degrees
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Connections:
- net /FT2232/_nPWREN renamed /FT2232/_PWREN
- net /FT2232/nPWREN renamed /FT2232/PWREN
- C14 pad 2: GND -> GNDA
- R57 pad 2: +3.3V -> GND
- R58 pad 2: +3.3V -> GND
- R65 pad 2: +3.3V -> GND
- U6 pad 18: /SHOST_SSRXP -> /SHOST_SSRXN
- U6 pad 19: /SHOST_SSRXN -> /SHOST_SSRXP
- U6 pad 21: (no net) -> GND
- U7 pad 7: /FT2232_DP -> /FT2232_DN
- U7 pad 8: /FT2232_DN -> /FT2232_DP
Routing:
- net /NRST: track 0.00 -> 223.5 mm, vias 0 -> 5
- net /board_control/CC1: track 0.00 -> 185.5 mm, vias 0 -> 6
- net /board_control/CC2: track 0.00 -> 184.8 mm, vias 0 -> 6
- net /BUTTON: track 0.00 -> 178.4 mm
- net /nRESET_OUT: track 0.00 -> 170.8 mm, vias 0 -> 2
- net /USB_SEL: track 0.00 -> 159.3 mm, vias 0 -> 3
- net /USB_OEn: track 0.00 -> 159.0 mm, vias 0 -> 2
- net /LED2: track 0.00 -> 147.8 mm, vias 0 -> 3
- net /LED0: track 0.00 -> 143.5 mm, vias 0 -> 3
- net /LED1: track 0.00 -> 143.2 mm, vias 0 -> 3
- net /USB_PW_DUT: track 0.00 -> 129.4 mm, vias 0 -> 2
- net /FT2232_EECS: track 0.00 -> 120.9 mm, vias 0 -> 2
- net GND: track 0.00 -> 120.6 mm, vias 0 -> 92
- net /CURRENT_SENSE: track 0.00 -> 118.1 mm, vias 0 -> 2
- net /USB_PW_HOST: track 0.00 -> 115.1 mm, vias 0 -> 2
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- added copper zone on In1.Cu, net +3.3V
- added copper zone on F.Cu, net /USB_STORAGE_MUX/VBUS_DUT
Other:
- board text added: "J2 J1 12V ATX 5V ATX 5V ATX"
- board text added: "PWREN"
- board text removed: "DUT connections"
- board text removed: "J2 J1 12V ATX 5V ATX 5V"
- board text removed: "PWREN#"

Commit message: Continued routing
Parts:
- J1, J5: footprint Connector_USB:USB_C_Receptacle_G-Switch_GT-USB-7010ASV -> FOOTPRINTS:USB_C_Receptacle_G-Switch_GT-USB-7010ASV_fix
- moved R28 80.9 mm to (176.2, 122.1), turned to 90 degrees
- moved R27 79.7 mm to (178.6, 118.4)
- moved Q3 79.7 mm to (178.6, 122.1)
- moved 3v1 16.1 mm to (77.8, 107.0)
- moved C87 13.2 mm to (78.1, 105.4), turned to 180 degrees
- moved C65 12.2 mm to (152.1, 128.7)
- moved C88 11.2 mm to (77.9, 104.0), turned to 180 degrees
- moved C83 11.1 mm to (77.8, 92.1), turned to -90 degrees
- moved 3v3A1 9.38 mm to (174.8, 86.8)
- moved C84 8.86 mm to (80.0, 92.2), turned to -90 degrees
- moved C22 8.65 mm to (106.8, 179.4), turned to -90 degrees
- moved R17 7.39 mm to (150.1, 135.8), turned to 0 degrees
- moved R18 7.27 mm to (162.0, 133.1), turned to -90 degrees
- moved R8 6.43 mm to (161.8, 86.2), turned to 180 degrees
- moved TP11 6.23 mm to (158.5, 88.4)
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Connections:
- C13 pad 2: GND -> GNDA
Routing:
- net /board_control/VCCOUT: track 18.5 -> 333.9 mm, vias 0 -> 30
- net +5V: track 47.7 -> 254.2 mm, vias 0 -> 4
- net /USB_STORAGE_MUX/VBUS_STORAGE: track 63.1 -> 212.9 mm, vias 0 -> 12
- net /ON_OFF: track 1.44 -> 144.7 mm, vias 0 -> 3
- net GND: track 120.6 -> 212.3 mm, vias 92 -> 218
- net /USB 3.2 Gen2 front-hub/VBUS_MON_UP: track 0.00 -> 71.2 mm, vias 0 -> 4
- net /USB_PW_HOST: track 115.1 -> 49.9 mm
- net VCORE: track 27.8 -> 89.3 mm, vias 1 -> 19
- net /board_control/_VCC: track 0.00 -> 60.4 mm
- net /board_control/VCCOUT_SW: track 0.00 -> 50.7 mm
- net /FT2232_EEDATA: track 45.3 -> 92.5 mm, vias 1 -> 2
- net +3.3V: track 98.1 -> 138.1 mm, vias 38 -> 53
- net Net-(J1-SHIELD): track 0.00 -> 29.4 mm
- net Net-(J8-SHIELD): track 0.00 -> 27.5 mm, vias 0 -> 2
- net VCC: track 0.00 -> 27.3 mm
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- added copper zone on F.Cu, net +3.3V
- added copper zone on F.Cu, net +5V
- added copper zone on F.Cu, net /Power/LVCORE
- added copper zone on F.Cu, net /Power/LVCORE3
- added copper zone on F.Cu, net /board_control/_VCC
- added copper zone on F.Cu, net GND
- added copper zone on F.Cu, net VCORE
- added copper zone on In1.Cu, net VCORE

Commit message: Almost ready 2.0.0
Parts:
- added REF**: Symbol_Barrel_Polarity, Symbol:Symbol_Barrel_Polarity, F.Cu at (91.1, 202.7)
- added REF**: OSHW-Logo2_14.6x12mm_SilkScreen, Symbol:OSHW-Logo2_14.6x12mm_SilkScreen, F.Cu at (203.7, 169.0)
- added REF**: Symbol_Barrel_Polarity, Symbol:Symbol_Barrel_Polarity, F.Cu at (163.4, 75.3)
- C1, C10, C11, C12, C2, C3, C31, C4, C59, C6, C60, C65, C73, C75, C79, C83, C85, C88, C89, C99: footprint Capacitor_SMD:C_0603_1608Metric_Pad1.08x0.95mm_HandSolder -> Capacitor_SMD:C_0603_1608Metric
- C19, C21: footprint Capacitor_SMD:C_0402_1005Metric -> Capacitor_SMD:C_0603_1608Metric
- J28: value CASE CONNECTORS -> 6x2 2.54mm header
- R10: value 4k7 -> 10k
- R26: value 49K9 -> 49K9 1%
- R32: value 12k -> 12k 1%
- R42: value 22k -> 22k 1%
- R43: value 5k1 -> 5k1 1%
- R55: value 10K -> 10k
- R8: value 2k4 -> 2k4 1%
- R9: value 470 -> 470 1%
- U5: value ~ -> TMUXHS221
- Y3: value 12MHz crystal +/- 30ppm max 12pf -> Cristales 12.000 MHZ 10PF
- moved R118 3.58 mm to (174.6, 196.8), turned to 90 degrees
- moved C21 2.89 mm to (106.9, 176.7), turned to 90 degrees
- moved R72 2.16 mm to (128.9, 157.6)
- moved R71 2.16 mm to (127.8, 157.6)
- moved REF** 2.08 mm to (63.8, 217.3)
- moved REF** 1.82 mm to (63.7, 206.1)
- moved C19 0.98 mm to (109.2, 163.8)
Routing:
- net +1V8: track 11.8 -> 49.5 mm, vias 1 -> 4
- net GND: track 212.3 -> 241.6 mm, vias 218 -> 233
- net Net-(J5-SHIELD): track 0.00 -> 21.6 mm
- net +3.3V: track 138.1 -> 152.4 mm, vias 53 -> 57
- net Net-(J8-SHIELD): track 27.5 -> 39.3 mm
- net Net-(D8-K): track 8.89 -> 13.1 mm
- net /board_control/VCCOUT: track 333.9 -> 337.9 mm, vias 30 -> 31
- net Net-(U8-USB3DN_RXDP4): track 5.13 -> 7.25 mm
- net Net-(U8-USB3DN_RXDM4): track 4.87 -> 6.98 mm
- net GNDA: track 18.5 -> 20.5 mm
- net /FT2232/BC7: track 54.1 -> 55.7 mm
- net Net-(D9-K): track 13.6 -> 14.4 mm
- removed copper zone on In1.Cu, net GND
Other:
- board text added: "USBPD OUT"
- board text removed: "USBPD_OUT 5-20V"
